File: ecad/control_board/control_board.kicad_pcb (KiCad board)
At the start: 2 copper layers, 40 x 40 mm, 31 parts, among them J1 USB_C_Receptacle_USB2.0_16P, J2 JST SH, U1 W25Q16JVUXIQ, U2 NCP1117-3.3_SOT223, U3 RP2040, Y1 ABM8-272-T3

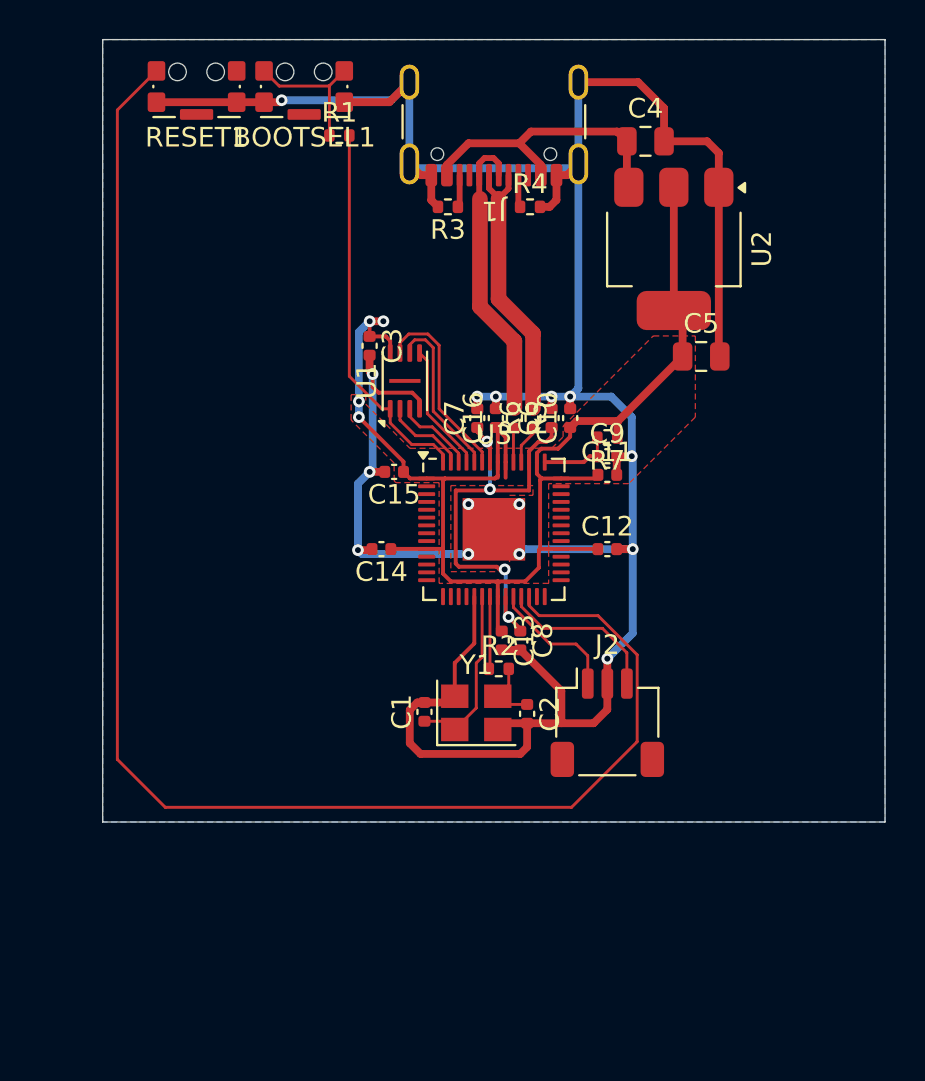
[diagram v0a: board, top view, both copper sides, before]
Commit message: Makes a control_board
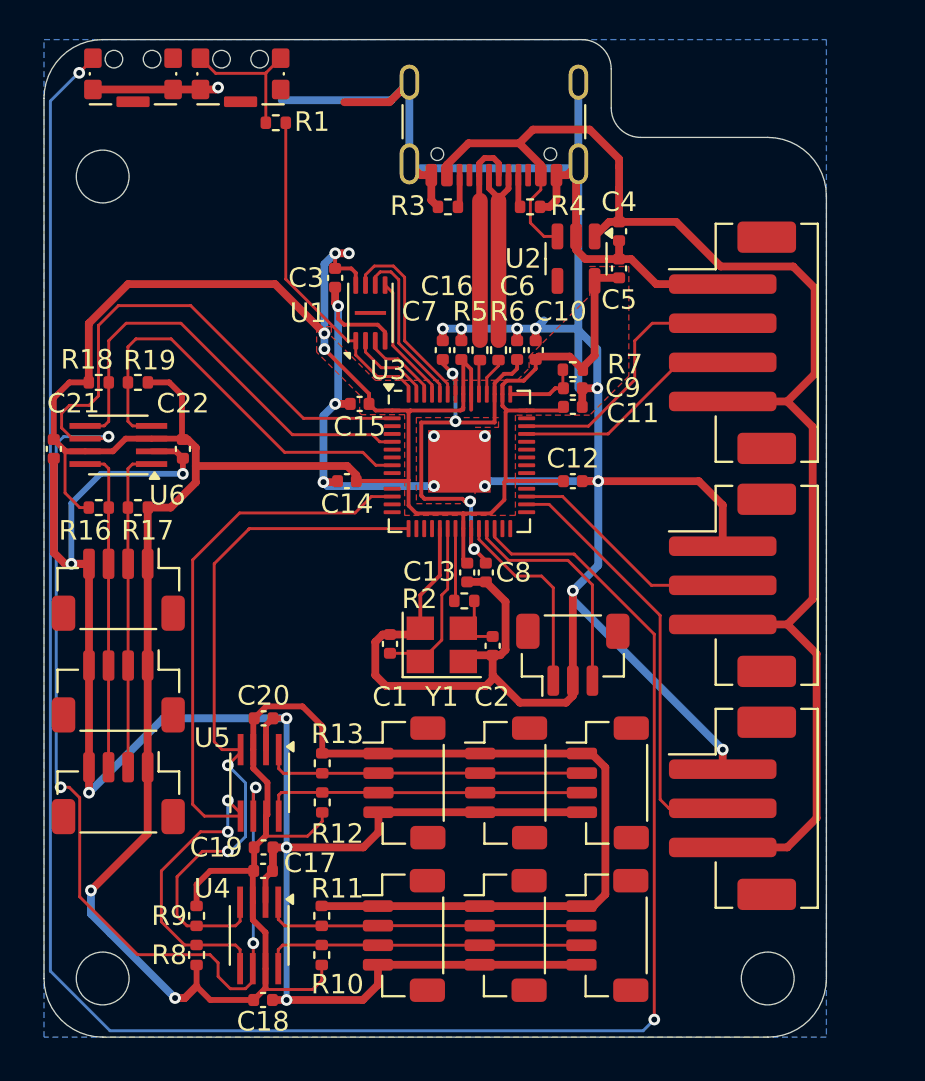
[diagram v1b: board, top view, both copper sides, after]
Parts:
- added C17: 100n, Capacitor_SMD:C_0402_1005Metric, F.Cu at (118.2, 92.5)
- added C18: 100n, Capacitor_SMD:C_0402_1005Metric, F.Cu at (118.2, 99.1)
- added C19: 100n, Capacitor_SMD:C_0402_1005Metric, F.Cu at (118.2, 91.3)
- added C20: 100n, Capacitor_SMD:C_0402_1005Metric, F.Cu at (118.2, 84.7)
- added C21: 100n, Capacitor_SMD:C_0402_1005Metric, F.Cu at (107.5, 70.9)
- added C22: 100n, Capacitor_SMD:C_0402_1005Metric, F.Cu at (114.1, 70.9)
- added J10: JST SH 4, woodpecker:JST_SH_BM04B-SRSS-TB_1x04-1MP_P1.00mm_Vertical, F.Cu at (130.6, 88.0)
- added J11: JST SH 4, woodpecker:JST_SH_BM04B-SRSS-TB_1x04-1MP_P1.00mm_Vertical, F.Cu at (125.4, 88.0)
- added J12: JST PH 4, woodpecker:JST_PH_B4B-PH-SM4-TB_1x04-1MP_P2.00mm_Vertical, F.Cu at (142.2, 65.5)
- added J13: JST PH 3, woodpecker:JST_PH_B3B-PH-SM4-TB_1x03-1MP_P2.00mm_Vertical, F.Cu at (142.2, 77.9)
- added J14: JST PH 3, woodpecker:JST_PH_B3B-PH-SM4-TB_1x03-1MP_P2.00mm_Vertical, F.Cu at (142.2, 89.3)
- added J3: JST SH 4, woodpecker:JST_SH_BM04B-SRSS-TB_1x04-1MP_P1.00mm_Vertical, F.Cu at (110.8, 83.3)
- added J4: JST SH 4, woodpecker:JST_SH_BM04B-SRSS-TB_1x04-1MP_P1.00mm_Vertical, F.Cu at (110.8, 88.5)
- added J5: JST SH 4, woodpecker:JST_SH_BM04B-SRSS-TB_1x04-1MP_P1.00mm_Vertical, F.Cu at (110.8, 78.1)
- added J6: JST SH 4, woodpecker:JST_SH_BM04B-SRSS-TB_1x04-1MP_P1.00mm_Vertical, F.Cu at (135.8, 95.8)
- added J7: JST SH 4, woodpecker:JST_SH_BM04B-SRSS-TB_1x04-1MP_P1.00mm_Vertical, F.Cu at (125.4, 95.8)
- added J8: JST SH 4, woodpecker:JST_SH_BM04B-SRSS-TB_1x04-1MP_P1.00mm_Vertical, F.Cu at (130.6, 95.8)
- added J9: JST SH 4, woodpecker:JST_SH_BM04B-SRSS-TB_1x04-1MP_P1.00mm_Vertical, F.Cu at (135.8, 88.0)
- added R10: 2.2k, Resistor_SMD:R_0402_1005Metric, F.Cu at (121.2, 96.8)
- added R11: 2.2k, Resistor_SMD:R_0402_1005Metric, F.Cu at (121.2, 94.8)
- added R12: 2.2k, Resistor_SMD:R_0402_1005Metric, F.Cu at (121.2, 89.0)
- added R13: 2.2k, Resistor_SMD:R_0402_1005Metric, F.Cu at (121.2, 87.0)
- added R16: 2.2k, Resistor_SMD:R_0402_1005Metric, F.Cu at (109.8, 73.9)
- added R17: 2.2k, Resistor_SMD:R_0402_1005Metric, F.Cu at (111.8, 73.9)
- added R18: 5.1k, Resistor_SMD:R_0402_1005Metric, F.Cu at (109.8, 67.5)
- added R19: 5.1k, Resistor_SMD:R_0402_1005Metric, F.Cu at (111.8, 67.5)
- added R8: 5.1k, Resistor_SMD:R_0402_1005Metric, F.Cu at (114.8, 96.8)
- added R9: 5.1k, Resistor_SMD:R_0402_1005Metric, F.Cu at (114.8, 94.8)
- added REF**: MountingHole_2.7mm_M2.5, MountingHole:MountingHole_2.7mm_M2.5, F.Cu at (110.0, 98.0)
- added REF**: MountingHole_2.7mm_M2.5, MountingHole:MountingHole_2.7mm_M2.5, F.Cu at (144.0, 98.0)
- added REF**: MountingHole_2.7mm_M2.5, MountingHole:MountingHole_2.7mm_M2.5, F.Cu at (110.0, 57.0)
- added U4: TCA9406DCTR, Package_SO:SSOP-8_2.95x2.8mm_P0.65mm, F.Cu at (118.0, 95.8)
- added U5: TCA9406DCTR, Package_SO:SSOP-8_2.95x2.8mm_P0.65mm, F.Cu at (118.0, 88.0)
- added U6: TCA9406DCTR, Package_SO:SSOP-8_2.95x2.8mm_P0.65mm, F.Cu at (110.8, 70.7)
- C4, C5: value 10u -> 2u2; footprint Capacitor_SMD:C_0805_2012Metric -> Capacitor_SMD:C_0402_1005Metric
- J2: value JST SH -> JST SH 3; footprint Connector_JST:JST_SH_SM03B-SRSS-TB_1x03-1MP_P1.00mm_Horizontal -> woodpecker:JST_SH_BM03B-SRSS-TB_1x03-1MP_P1.00mm_Vertical
- U2: value NCP1117-3.3_SOT223 -> TLV75733PDBV; footprint Package_TO_SOT_SMD:SOT-223-3_TabPin2 -> Package_TO_SOT_SMD:SOT-23-5
- moved C5 6.16 mm to (136.4, 61.7), turned to 90 degrees
- moved U2 5.02 mm to (134.2, 61.2)
- moved C4 4.79 mm to (136.4, 59.8), turned to -90 degrees
- moved C1 3.90 mm to (124.7, 80.9)
- moved C3 3.90 mm to (121.9, 62.2)
- moved U1 3.90 mm to (123.7, 64.0)
- moved C10 3.90 mm to (132.1, 65.9)
- moved C11 3.90 mm to (134.0, 68.8)
- moved C12 3.90 mm to (134.0, 72.6)
- moved C13 3.90 mm to (128.6, 77.2)
- moved C9 3.90 mm to (134.0, 67.8)
- moved J2 3.90 mm to (134.0, 81.5)
- moved R5 3.90 mm to (129.3, 65.9)
- moved R7 3.90 mm to (134.0, 66.9)
- moved R2 3.90 mm to (128.5, 78.7)
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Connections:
- U2 pad 1: GND -> +5V
- U2 pad 2: +3V3 -> GND
- U3 pad 12: unconnected-(U3-GPIO9-Pad12) -> /I2C0/SCL
- U3 pad 15: unconnected-(U3-GPIO12-Pad15) -> /I2C0/SDA
- U3 pad 2: unconnected-(U3-GPIO0-Pad2) -> /I2C_E
- U3 pad 30: unconnected-(U3-GPIO19-Pad30) -> /BOT/DOUT
- U3 pad 31: unconnected-(U3-GPIO20-Pad31) -> /MID/DOUT
- U3 pad 39: unconnected-(U3-GPIO27_ADC1-Pad39) -> /TOP/DOUT
- U3 pad 40: unconnected-(U3-GPIO28_ADC2-Pad40) -> /TOP/SDOUT
- U3 pad 5: unconnected-(U3-GPIO3-Pad5) -> /I2C1/SCL
- U3 pad 8: unconnected-(U3-GPIO6-Pad8) -> /I2C1/SDA
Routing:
- net +3V3: track 70.1 -> 215.3 mm, vias 4 -> 6
- net GND: track 163.5 -> 278.7 mm, vias 15 -> 22
- net /I2C_E: track 0.00 -> 76.7 mm, vias 0 -> 4
- net +5V: track 15.1 -> 74.7 mm
- net /I2C0/SCL: track 0.00 -> 41.8 mm, vias 0 -> 2
- net /I2C0/SDA: track 0.00 -> 37.2 mm, vias 0 -> 2
- net /RUN: track 76.5 -> 110.3 mm, vias 0 -> 2
- net /I2C1/SCL: track 0.00 -> 22.8 mm
- net /BOT/DOUT: track 0.00 -> 22.0 mm
- net /I2C1/SDA: track 0.00 -> 21.5 mm
- net /BOT/SCL: track 0.00 -> 16.6 mm
- net /BOT/SDA: track 0.00 -> 16.6 mm
- net /MID/SCL: track 0.00 -> 16.6 mm
- net /MID/SDA: track 0.00 -> 16.6 mm
- net /TOP/SCL: track 0.00 -> 16.6 mm
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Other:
- board size 40 x 40 mm -> 40 x 51 mm

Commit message: Updates boards
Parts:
- BOOTSEL1, RESET1: footprint Button_Switch_SMD:SW_SPST_CK_KMS2xxGP -> woodpecker:SW_SPST_CK_KMS2xxGP
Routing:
- net /RUN: track 110.3 -> 115.1 mm
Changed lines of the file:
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@@
 		(pad_to_mask_clearance 0)
 		(allow_soldermask_bridges_in_footprints no)
+		(aux_axis_origin 130 50)
 		(grid_origin 130 50)
 		(pcbplotparams
@@
 		(tags "resistor")
 		(property "Reference" "R17"
-			(at -0.5 -1.17 360)
+			(at -0.5 -1.17 0)
 			(layer "F.SilkS")
 			(effects
@@
 		)
 		(property "Value" "2.2k"
-			(at 0 1.17 360)
+			(at 0 1.17 0)
 			(layer "F.Fab")
 			(effects
@@
 		)
 		(fp_text user "${REFERENCE}"
-			(at 0 0 360)
+			(at 0 0 0)
 			(layer "F.Fab")
 			(effects
@@
 		)
 		(property "Value" "100n"
-			(at 0 1.16 360)
+			(at 0 1.16 0)
 			(layer "F.Fab")
 			(effects
@@
 		)
 		(fp_text user "${REFERENCE}"
-			(at 0 0 360)
+			(at 0 0 0)
 			(layer "F.Fab")
 			(effects
@@
 		(tags "capacitor")
 		(property "Reference" "C18"
-			(at 0 1.1 360)
+			(at 0 1.1 0)
 			(layer "F.SilkS")
 			(effects
@@
 		)
 		(property "Value" "100n"
-			(at 0 1.16 360)
+			(at 0 1.16 0)
 			(layer "F.Fab")
 			(effects
@@
 		)
 		(fp_text user "${REFERENCE}"
-			(at 0 0 360)
+			(at 0 0 0)
 			(layer "F.Fab")
 			(effects
@@
 		(tags "resistor")
 		(property "Reference" "R19"
-			(at -0.6 1.125 360)
+			(at -0.6 1.125 0)
 			(layer "F.SilkS")
 			(effects
@@
 		)
 		(property "Value" "5.1k"
-			(at 0 1.17 360)
+			(at 0 1.17 0)
 			(layer "F.Fab")
 			(effects
@@
 		)
 		(fp_text user "${REFERENCE}"
-			(at 0 0 360)
+			(at 0 0 0)
 			(layer "F.Fab")
 			(effects
@@
 		(tags "capacitor")
 		(property "Reference" "C19"
-			(at -2.425 0 360)
+			(at -2.425 0 0)
 			(layer "F.SilkS")
 			(effects
@@
 		)
 		(property "Value" "100n"
-			(at 0 1.16 360)
+			(at 0 1.16 0)
 			(layer "F.Fab")
 			(effects
@@
 		)
 		(fp_text user "${REFERENCE}"
-			(at 0 0 360)
+			(at 0 0 0)
 			(layer "F.Fab")
 			(effects
@@
 		(tags "resistor")
 		(property "Reference" "R16"
-			(at -0.7 1.175 360)
+			(at -0.7 1.175 0)
 			(layer "F.SilkS")
 			(effects
@@
 		)
 		(property "Value" "2.2k"
-			(at 0 1.17 360)
+			(at 0 1.17 0)
 			(layer "F.Fab")
 			(effects
@@
 		)
 		(fp_text user "${REFERENCE}"
-			(at 0 0 360)
+			(at 0 0 0)
 			(layer "F.Fab")
 			(effects
@@
 		)
 	)
-	(footprint "Button_Switch_SMD:SW_SPST_CK_KMS2xxGP"
+	(footprint "woodpecker:SW_SPST_CK_KMS2xxGP"
 		(layer "F.Cu")
 		(at 117.05 51.75 180)
@@
 		(tags "Switch SPST KMS2")
 		(property "Reference" "BOOTSEL1"
-			(at 0 -2.6 0)
+			(at 0 -2.6 180)
 			(layer "F.SilkS")
-			(hide yes)
 			(effects
 				(font
@@
 		)
 		(property "Value" "CK_KMS2xxG"
-			(at 0 3.2 0)
+			(at 0 3.2 180)
 			(layer "F.Fab")
 			(effects
@@
 			)
 		)
-		(property "Footprint" "Button_Switch_SMD:SW_SPST_CK_KMS2xxGP"
+		(property "Footprint" "woodpecker:SW_SPST_CK_KMS2xxGP"
 			(at 0 0 180)
 			(unlocked yes)
@@
 		)
 		(fp_text user "${REFERENCE}"
-			(at 0 0 0)
+			(at 0 0 180)
 			(layer "F.Fab")
 			(effects
@@
 			(pintype "passive")
 		)
-		(model "${KICAD8_3DMODEL_DIR}/Button_Switch_SMD.3dshapes/SW_SPST_CK_KMS2xxGP.wrl"
+		(model "${KIPRJMOD}/../libs/woodpecker.3dsymbols/KMS231GPLFS.stp"
 			(offset
 				(xyz 0 0 0)
@@
 			)
 			(rotate
-				(xyz 0 0 0)
+				(xyz -90 0 0)
 			)
 		)
@@
 		(tags "capacitor")
 		(property "Reference" "C20"
-			(at 0 -1.16 360)
+			(at 0 -1.16 0)
 			(layer "F.SilkS")
 			(effects
@@
 		)
 		(property "Value" "100n"
-			(at 0 1.16 360)
+			(at 0 1.16 0)
 			(layer "F.Fab")
 			(effects
@@
 		)
 		(fp_text user "${REFERENCE}"
-			(at 0 0 360)
+			(at 0 0 0)
 			(layer "F.Fab")
 			(effects
@@
 		(tags "resistor")
 		(property "Reference" "R18"
-			(at -0.6 -1.17 360)
+			(at -0.6 -1.17 0)
 			(layer "F.SilkS")
 			(effects
@@
 		)
 		(property "Value" "5.1k"
-			(at 0 1.17 360)
+			(at 0 1.17 0)
 			(layer "F.Fab")
 			(effects
@@
 		)
 		(fp_text user "${REFERENCE}"
-			(at 0 0 360)
+			(at 0 0 0)
 			(layer "F.Fab")
 			(effects
@@
 		)
 	)
-	(footprint "Button_Switch_SMD:SW_SPST_CK_KMS2xxGP"
+	(footprint "woodpecker:SW_SPST_CK_KMS2xxGP"
 		(layer "F.Cu")
 		(at 111.55 51.75 180)
@@
 		(tags "Switch SPST KMS2")
 		(property "Reference" "RESET1"
-			(at 0 -2.6 0)
+			(at 0 -2.6 180)
 			(layer "F.SilkS")
-			(hide yes)
 			(effects
 				(font
@@
 		)
 		(property "Value" "CK_KMS2xxG"
-			(at 0 3.2 0)
+			(at 0 3.2 180)
 			(layer "F.Fab")
 			(effects
@@
 			)
 		)
-		(property "Footprint" "Button_Switch_SMD:SW_SPST_CK_KMS2xxGP"
+		(property "Footprint" "woodpecker:SW_SPST_CK_KMS2xxGP"
 			(at 0 0 180)
 			(unlocked yes)
@@
 		)
 		(fp_text user "${REFERENCE}"
-			(at 0 0 0)
+			(at 0 0 180)
 			(layer "F.Fab")
 			(effects
@@
 			(pintype "passive")
 		)
-		(model "${KICAD8_3DMODEL_DIR}/Button_Switch_SMD.3dshapes/SW_SPST_CK_KMS2xxGP.wrl"
+		(model "${KIPRJMOD}/../libs/woodpecker.3dsymbols/KMS231GPLFS.stp"
 			(offset
 				(xyz 0 0 0)
@@
 			)
 			(rotate
-				(xyz 0 0 0)
+				(xyz -90 0 0)
 			)
 		)
@@
 		(tags "SSOP-8 2.95x2.8mm Pitch 0.65mm")
 		(property "Reference" "U6"
-			(at -2.5 -2.575 360)
+			(at -2.5 -2.575 0)
 			(layer "F.SilkS")
 			(effects
@@
 		)
 		(property "Value" "TCA9406DCTR"
-			(at 0 2.6 360)
+			(at 0 2.6 0)
 			(layer "F.Fab")
 			(effects
@@
 		)
 		(fp_text user "${REFERENCE}"
-			(at 0 0 360)
+			(at 0 0 0)
 			(layer "F.Fab")
 			(effects
@@
 	)
 	(segment
+		(start 110.275 51.725)
+		(end 112.825 51.725)
+		(width 0.15)
+		(layer "F.Cu")
+		(net 14)
+	)
+	(segment
 		(start 109.5 51)
 		(end 108.8 51.7)
@@
 		(width 0.15)
 		(layer "F.Cu")
+		(net 14)
+	)
+	(segment
+		(start 112.825 51.725)
+		(end 113.6 50.95)
+		(width 0.15)
+		(layer "F.Cu")
+		(net 14)
+	)
+	(segment
+		(start 109.5 50.95)
+		(end 110.275 51.725)
+		(width 0.15)
+		(layer "F.Cu")

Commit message: [WIP] control board
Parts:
- removed C20, C21, C22: 100n, Capacitor_SMD:C_0402_1005Metric
- removed J11, J8: JST SH 4, woodpecker:JST_SH_BM04B-SRSS-TB_1x04-1MP_P1.00mm_Vertical
- removed J12: JST PH 4, woodpecker:JST_PH_B4B-PH-SM4-TB_1x04-1MP_P2.00mm_Vertical
- removed J13, J14: JST PH 3, woodpecker:JST_PH_B3B-PH-SM4-TB_1x03-1MP_P2.00mm_Vertical
- removed R10, R11, R12, R13, R16, R17: 2.2k, Resistor_SMD:R_0402_1005Metric
- removed R18, R19, R9: 5.1k, Resistor_SMD:R_0402_1005Metric
- removed U6: TCA9406DCTR, Package_SO:SSOP-8_2.95x2.8mm_P0.65mm
- added D1: 1N4148WS, Diode_SMD:D_SOD-323, F.Cu at (154.4, 41.5)
- added Q6: RE1C002UN, Package_TO_SOT_SMD:SOT-416, F.Cu at (75.5, 48.5)
- BOOTSEL1, RESET1: footprint woodpecker:SW_SPST_CK_KMS2xxGP -> Button_Switch_SMD:SW_SPST_CK_KMS2xxGP
- C9: value 2u2 -> 1u
- J10, J9: value JST SH 4 -> JST PH 3; footprint woodpecker:JST_SH_BM04B-SRSS-TB_1x04-1MP_P1.00mm_Vertical -> woodpecker:JST_PH_S3B-PH-SM4-TB_1x03-1MP_P2.00mm_Horizontal
- J2: footprint woodpecker:JST_SH_BM03B-SRSS-TB_1x03-1MP_P1.00mm_Vertical -> woodpecker:JST_SH_SM03B-SRSS-TB_1x03-1MP_P1.00mm_Horizontal
- J3, J4, J5, J6, J7: value JST SH 4 -> JST SH 3; footprint woodpecker:JST_SH_BM04B-SRSS-TB_1x04-1MP_P1.00mm_Vertical -> woodpecker:JST_SH_BM03B-SRSS-TB_1x03-1MP_P1.00mm_Vertical
- R3: value 5.1k -> 900k
- R4: value 5.1k -> 71k5
- R7: value 200 -> 27k
- R8: value 5.1k -> 27k
- U4: value TCA9406DCTR -> TUSB320I; footprint Package_SO:SSOP-8_2.95x2.8mm_P0.65mm -> Package_DFN_QFN:Texas_X2QFN-12_1.6x1.6mm_P0.4mm
- U5: value TCA9406DCTR -> TPS2552DRV; footprint Package_SO:SSOP-8_2.95x2.8mm_P0.65mm -> woodpecker:Texas_WSON-6-1EP_2x2mm_P0.65mm_EP1x1.6mm_ThermalVias
- moved C18 67.8 mm to (79.8, 43.2)
- moved R8 66.1 mm to (76.4, 43.0)
- moved U4 64.1 mm to (151.0, 40.9)
- moved C19 62.7 mm to (76.2, 44.8)
- moved C17 62.3 mm to (152.9, 40.8), turned to -90 degrees
- moved R7 60.0 mm to (76.1, 51.2)
- moved R4 57.3 mm to (76.2, 44.8)
- moved U5 53.2 mm to (82.2, 48.7)
- moved R3 29.6 mm to (152.6, 42.5)
- moved J3 18.8 mm to (92.0, 84.5)
- moved J5 12.9 mm to (98.1, 80.5)
- moved C4 1.65 mm to (136.4, 61.5)
- moved C5 1.65 mm to (136.4, 63.4)
- moved U2 1.65 mm to (134.2, 62.9)
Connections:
- C17 pad 1: +3V3 -> VBUS_5V
- C18 pad 1: +3V3 -> VBUS
- C19 pad 1: +3V3 -> +5V_LED
- C9 pad 1: /3V3_ADC -> /VBUS_UNFLT
- J1 pad A4: +5V -> /VBUS_UNFLT
- J1 pad A9: +5V -> /VBUS_UNFLT
- J1 pad B4: +5V -> /VBUS_UNFLT
- J1 pad B9: +5V -> /VBUS_UNFLT
- J10 pad 1: +3V3 -> +5V
- J10 pad 2: /BOT/SDA -> /LED_OUT1
- J10 pad 3: /BOT/SCL -> GND
- J3 pad 2: /MID/SDA -> /RX1
- J3 pad 3: /MID/SCL -> GND
- J4 pad 2: /MID/SDA -> /RX2
- J4 pad 3: /MID/SCL -> GND
- J5 pad 2: /MID/SDA -> /RX3
- J5 pad 3: /MID/SCL -> GND
- J6 pad 2: /TOP/SDA -> /RX4
- J6 pad 3: /TOP/SCL -> GND
- J7 pad 2: /TOP/SDA -> /RX5
- J7 pad 3: /TOP/SCL -> GND
- J9 pad 1: +3V3 -> +5V
- J9 pad 2: /BOT/SDA -> /LED_OUT0
- J9 pad 3: /BOT/SCL -> GND
- R3 pad 1: /CC2 -> VBUS
- R3 pad 2: GND -> Net-(U4-VBUS_DET)
- R4 pad 1: /CC1 -> Net-(U5-ILIM)
- R7 pad 1: +3V3 -> Net-(U5-ILIM)
- R7 pad 2: /3V3_ADC -> Net-(Q6-D)
- R8 pad 1: +3V3 -> /LED_FULL_EN
- R8 pad 2: /I2C0/SCL -> GND
- U3 pad 12: /I2C0/SCL -> unconnected-(U3-GPIO9-Pad12)
- U3 pad 15: /I2C0/SDA -> unconnected-(U3-GPIO12-Pad15)
- U3 pad 2: /I2C_E -> unconnected-(U3-GPIO0-Pad2)
- U3 pad 30: /BOT/DOUT -> unconnected-(U3-GPIO19-Pad30)
- U3 pad 31: /MID/DOUT -> unconnected-(U3-GPIO20-Pad31)
- U3 pad 39: /TOP/DOUT -> unconnected-(U3-GPIO27_ADC1-Pad39)
- U3 pad 40: /TOP/SDOUT -> unconnected-(U3-GPIO28_ADC2-Pad40)
- U3 pad 43: /3V3_ADC -> unconnected-(U3-ADC_AVDD-Pad43)
- U3 pad 5: /I2C1/SCL -> unconnected-(U3-GPIO3-Pad5)
- U3 pad 8: /I2C1/SDA -> unconnected-(U3-GPIO6-Pad8)
- U4 pad 1: /TOP/SDA -> /CC1
- U4 pad 2: GND -> /CC2
- U4 pad 3: +3V3 -> GND
- U4 pad 4: /I2C0/SDA -> Net-(U4-VBUS_DET)
- U4 pad 5: /I2C0/SCL -> unconnected-(U4-ADDR-Pad5)
- U4 pad 6: /I2C_E -> unconnected-(U4-~{INT}/OUT3-Pad6)
- U4 pad 7: +3V3 -> /USB_OUT1
- U4 pad 8: /TOP/SCL -> /USB_OUT2
- U5 pad 1: /BOT/SDA -> +5V_LED
- U5 pad 2: GND -> Net-(U5-ILIM)
- U5 pad 3: +3V3 -> /~{LED_FAULT}
- U5 pad 4: /I2C0/SDA -> GND
- U5 pad 5: /I2C0/SCL -> GND
- U5 pad 6: /I2C_E -> VBUS
- U5 pad 7: +3V3 -> GND
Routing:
- net GND: track 278.7 -> 66.0 mm, vias 22 -> 18
- net +3V3: track 215.3 -> 56.0 mm, vias 6 -> 4
- net /I2C_E: track 76.7 -> 0.00 mm, vias 4 -> 0
- net +5V: track 74.7 -> 0.00 mm
- net /I2C0/SCL: track 41.8 -> 0.00 mm, vias 2 -> 0
- net /I2C0/SDA: track 37.2 -> 0.00 mm, vias 2 -> 0
- net (no net): track 0.00 -> 25.8 mm
- net /I2C1/SCL: track 22.8 -> 0.00 mm
- net /BOT/DOUT: track 22.0 -> 0.00 mm
- net /I2C1/SDA: track 21.5 -> 0.00 mm
- net /BOT/SCL: track 16.6 -> 0.00 mm
- net /BOT/SDA: track 16.6 -> 0.00 mm
- net /MID/SCL: track 16.6 -> 0.00 mm
- net /MID/SDA: track 16.6 -> 0.00 mm
- net /TOP/SCL: track 16.6 -> 0.00 mm
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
